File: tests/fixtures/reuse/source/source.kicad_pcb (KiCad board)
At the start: 2 copper layers, 4 parts, among them U1 MCU

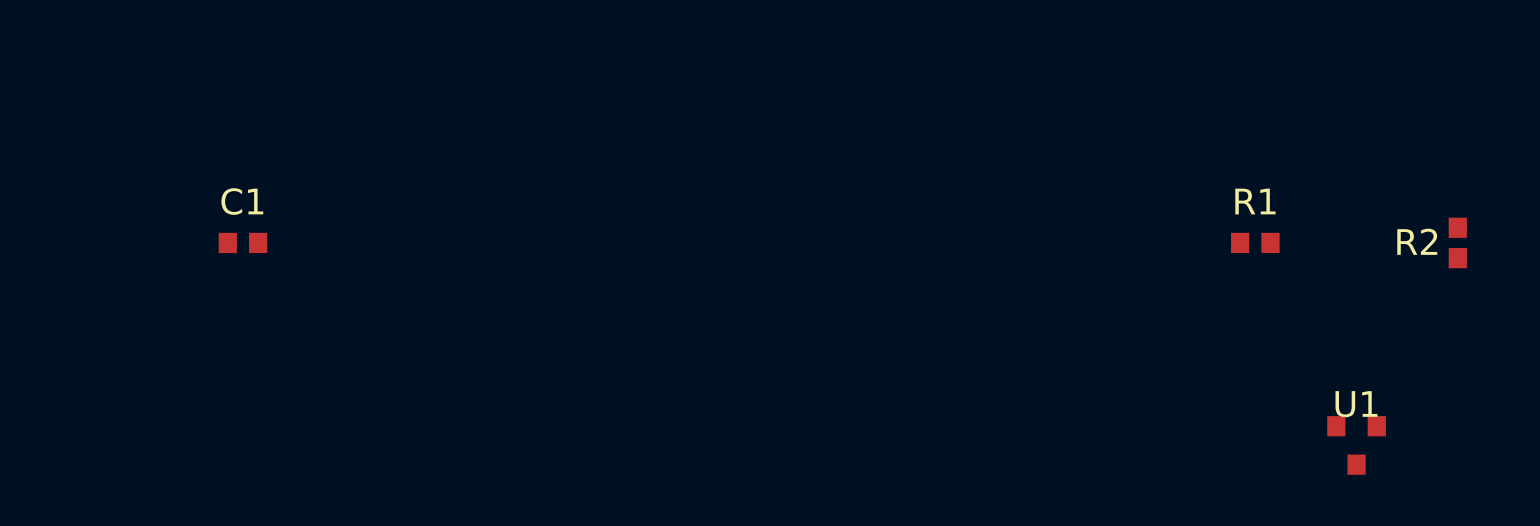
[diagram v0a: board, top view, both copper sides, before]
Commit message: feat(reuse): copy in-block tracks and vias (Slice 5) (#18)
Carries the routing half of the reuse pipeline through plan_apply and
the kicad_io write path so the source PCB's tracks and vias for a block
land in the target at the anchor-relative transform, with net names
rewritten through the per-block net_map. Boundary-crossing items are
surfaced on the plan's excluded_* lists so dry-run shows what's not
coming with. PRD slice 5 of issue #1.

Key decisions:
- Strict-boundary rule: a track is kept iff *both* endpoints land on an
  in-block footprint pad (within 1 um); a via is kept iff its position
  lands on an in-block pad. Items where one endpoint sits on an
  out-of-block pad go to excluded_*; items unrelated to the block are
  ignored.
- Tracks/vias are *appended* to the target's traceItems on apply.
  Idempotent re-apply (dedup against the lock) is Slice 8's territory.
- Fresh UUID4 tstamps are minted for appended items so kiutils can
  reparse the written file (an empty tstamp serializes as `(tstamp )`
  which fails on round-trip).
- Pad positions are now exposed on the typed Footprint so the block
  module can compute absolute pad positions without re-reading kiutils.

Files changed:
- src/kicad_blocks/kicad_io.py: add Track/ViaItem read models,
  TrackPlacement/ViaPlacement write models, pads on Footprint, extend
  apply_placements with tracks/vias kwargs, net-name validation.
- src/kicad_blocks/block.py: extend ApplyPlan with tracks/vias/
  excluded_*; new _plan_routing helper applies the strict-boundary rule
  and rewrites nets through net_map.
- src/kicad_blocks/reporter.py: render tracks/vias and exclusions in
  the apply-plan output.
- src/kicad_blocks/cli.py: pass routing through to apply_placements.
- tests/fixtures/reuse/source/source.kicad_pcb: add two in-block
  segments, one boundary-crossing segment, one in-block via, one
  out-of-block via.
- tests/test_kicad_io.py, tests/test_block.py, tests/test_reuse_cli.py:
  cover read, plan, exclusion, net-o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
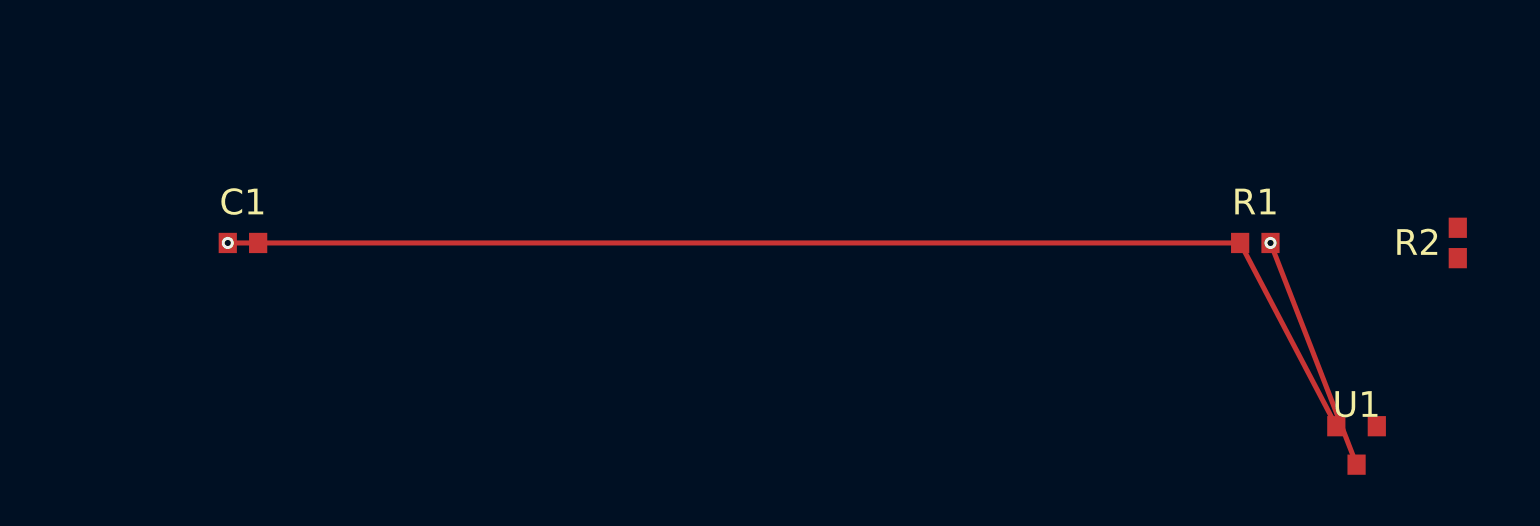
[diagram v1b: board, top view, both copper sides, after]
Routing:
- net +3V3: track 0.00 -> 60.2 mm, vias 0 -> 1
- net SIG: track 0.00 -> 11.7 mm, vias 0 -> 1
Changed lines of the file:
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@@
       (net 2 "GND"))
   )
+  (segment (start 100.75 50) (end 105 60.95) (width 0.25) (layer "F.Cu") (net 3))
+  (segment (start 99.25 50) (end 104 59.05) (width 0.25) (layer "F.Cu") (net 1))
+  (segment (start 49.25 50) (end 99.25 50) (width 0.25) (layer "F.Cu") (net 1))
+  (via (at 100.75 50) (size 0.6) (drill 0.3) (layers "F.Cu" "B.Cu") (net 3))
+  (via (at 49.25 50) (size 0.6) (drill 0.3) (layers "F.Cu" "B.Cu") (net 1))
 )

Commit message: feat(reuse): copy zones, board graphics, and check layer stackup (Slice 6) (#19)
Closes the reuse scope from PRD #1: copper zones and board-level
silkscreen/fab/courtyard graphics now travel with a block, filtered by a
padded AABB hull around the in-block footprint pads. Source/target layer
stackups are compared up front; mismatches raise ApplyError unless the
block opts in via `allow_layer_mismatch = true`. Cached zone fills are
dropped on copy so KiCAD repours on the target.

Key decisions:
- Hull = AABB of in-block pad positions + 5 mm margin (simpler than a
  convex hull, sufficient for typical blocks with surrounding silk/fab
  art). All-points-inside is the keep criterion; partial-overlap items
  are reported under `excluded_*` so dry-run surfaces them.
- ZonePlacement/GraphicPlacement carry an opaque kiutils reference plus
  a Transform; the deep-copy + coordinate rewrite happens inside
  apply_placements, keeping the "kiutils stays inside kicad_io"
  boundary intact.
- Stackup mismatch raises (hard refusal) rather than surfacing on the
  plan; with the override on, the diff appears as a plan warning.

Files changed:
- src/kicad_blocks/kicad_io.py — LayerInfo, ZoneItem, GraphicItem,
ZonePlacement, GraphicPlacement; Pcb.layers/zones/graphics; zone/graphic
  appender in apply_placements
- src/kicad_blocks/block.py — _plan_zones_and_graphics, hull AABB,
  _diff_layer_stackup, allow_layer_mismatch param
- src/kicad_blocks/config.py — allow_layer_mismatch field on BlockSpec
- src/kicad_blocks/cli.py — thread allow_layer_mismatch + zones/graphics
- src/kicad_blocks/reporter.py — render zones/graphics + excluded +
  layer-mismatch warning
- tests/fixtures/reuse/source/source.kicad_pcb — in-block GND zone +
  silk gr_text/gr_line + out-of-hull zone/text for exclusion coverage
- tests/test_block.py, test_kicad_io.py, test_config.py,
test_reuse_cli.py
  — unit + CLI coverage for every acceptance criterion

Blockers for next iteration: none.

Authored by: RALPH
Closes: 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
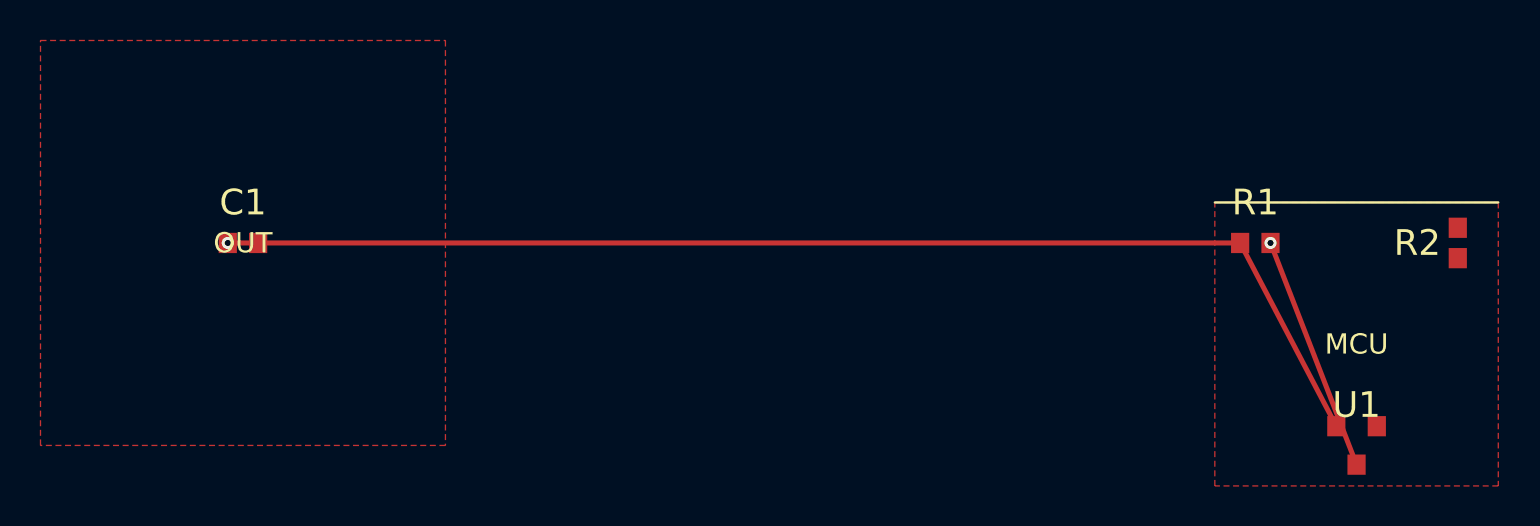
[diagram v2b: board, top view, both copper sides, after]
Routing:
- added copper zone on F.Cu, net (none)
- added copper zone on F.Cu, net GND
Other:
- board text added: "MCU"
- board text added: "OUT"
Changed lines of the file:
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@@
   (via (at 100.75 50) (size 0.6) (drill 0.3) (layers "F.Cu" "B.Cu") (net 3))
   (via (at 49.25 50) (size 0.6) (drill 0.3) (layers "F.Cu" "B.Cu") (net 1))
+  (gr_text "MCU" (at 105 55 0) (layer "F.SilkS") (effects (font (size 1 1) (thickness 0.15))))
+  (gr_line (start 98 48) (end 112 48) (width 0.12) (layer "F.SilkS"))
+  (gr_text "OUT" (at 50 50 0) (layer "F.SilkS") (effects (font (size 1 1) (thickness 0.15))))
+  (zone (net 2) (net_name "GND") (layer "F.Cu") (hatch edge 0.5) (connect_pads (clearance 0.25)) (min_thickness 0.25) (filled_areas_thickness no) (fill yes (thermal_gap 0.5) (thermal_bridge_width 0.5)) (polygon (pts (xy 98 48) (xy 112 48) (xy 112 62) (xy 98 62))))
+  (zone (net 0) (net_name "") (layer "F.Cu") (hatch edge 0.5) (connect_pads (clearance 0.25)) (min_thickness 0.25) (filled_areas_thickness no) (fill yes (thermal_gap 0.5) (thermal_bridge_width 0.5)) (polygon (pts (xy 40 40) (xy 60 40) (xy 60 60) (xy 40 60))))
 )
